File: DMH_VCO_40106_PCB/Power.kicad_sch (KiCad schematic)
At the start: 15 parts, among them J10 Panel_GND, J100 IDC_02x08, U1 40106, U2 TL074, U3 TL072

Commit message: Updates from testing on breadboard
- Removed Bus CV input, normalled it to V/oct input jack instead
- Renamed Lin FM input to Exp FM In 2
- Added annotations about temporary resistor/pot values
- Added annotations about pots and trimpots pinout
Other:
- company: (none) -> DMH Instruments
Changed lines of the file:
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@@
 	(generator_version "8.0")
 	(paper "A4")
+	(title_block
+		(company "DMH Instruments")
+	)
 	(junction
 		(at 142.24 31.75)

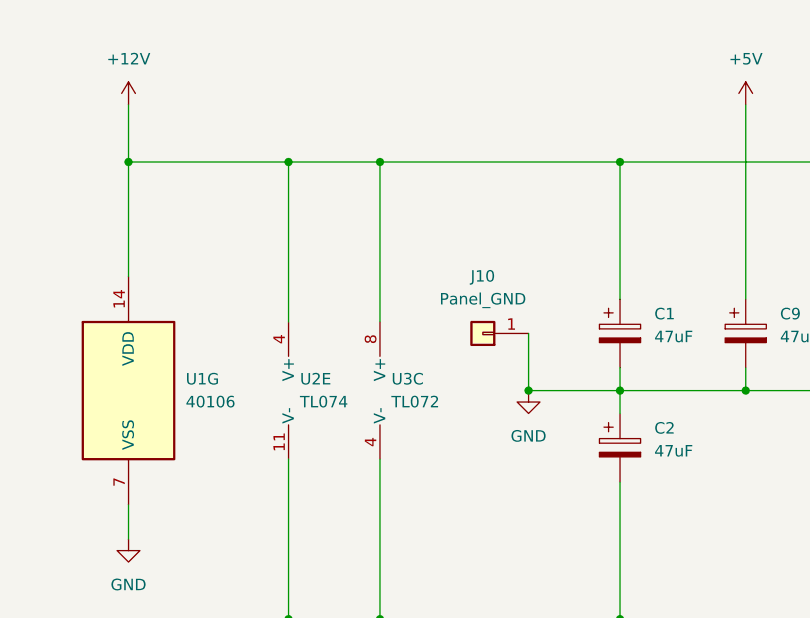
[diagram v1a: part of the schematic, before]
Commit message: Made U3 into TL074 instead of TL072
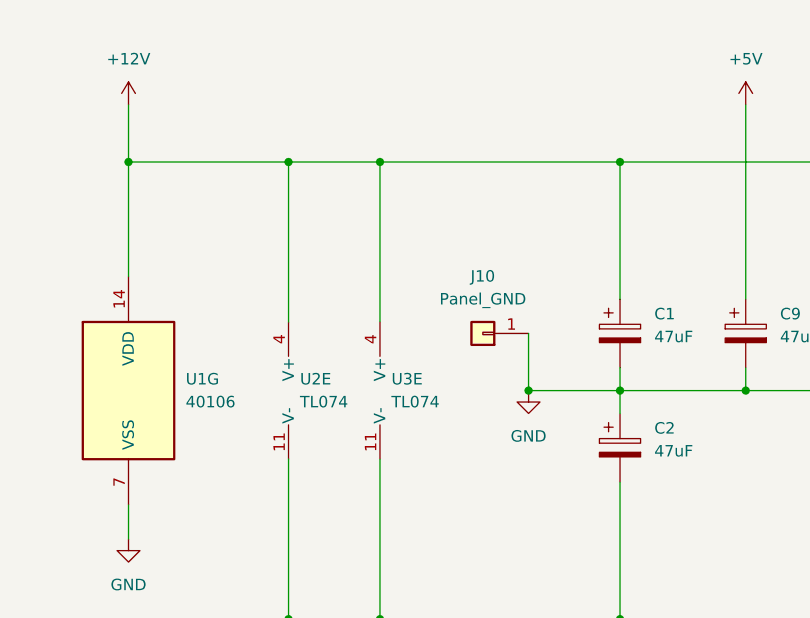
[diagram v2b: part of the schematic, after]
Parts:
- removed U3: TL072, Package_DIP:DIP-8_W7.62mm_Socket, symbol Amplifier_Operational:TL072
- added U3: TL074, symbol Amplifier_Operational:TL074
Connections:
- net +12V: now also U3.4 (V+)
- net -12V: now also U3.11 (V-)

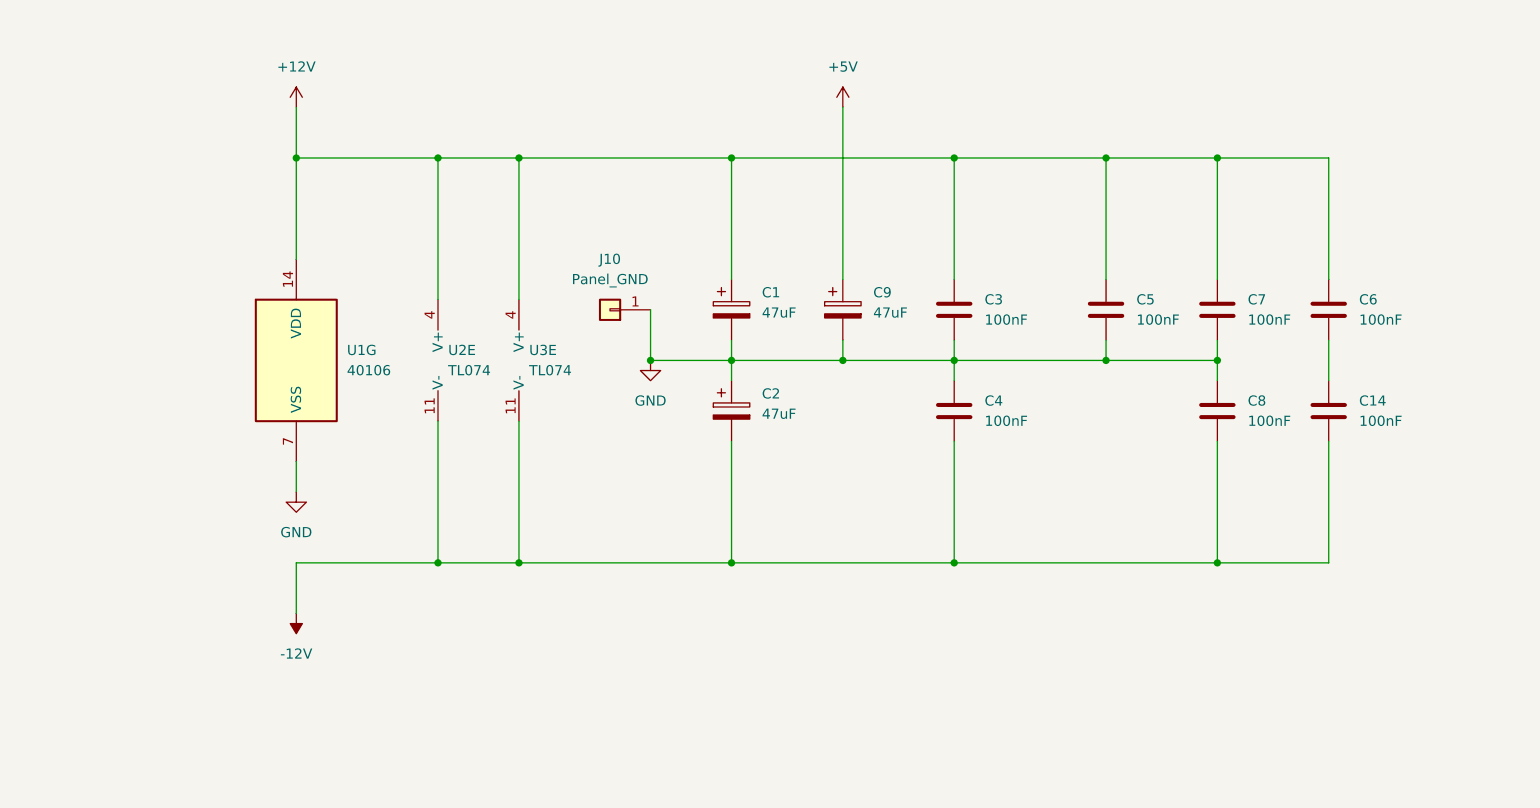
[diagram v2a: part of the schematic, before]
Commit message: Placed power for U4
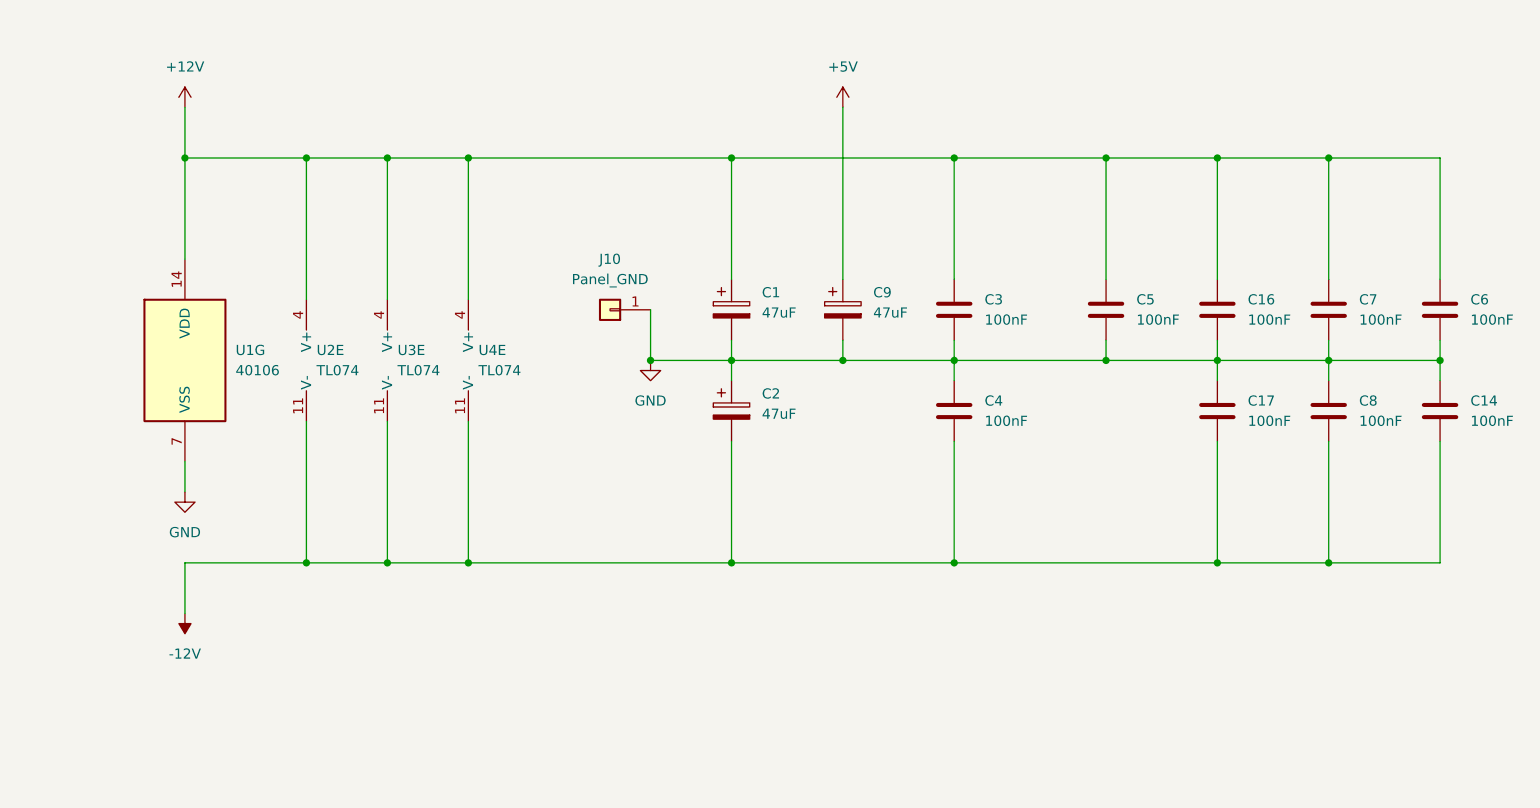
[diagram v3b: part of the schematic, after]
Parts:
- added C16, C17: 100nF, Capacitor_THT:C_Disc_D4.3mm_W1.9mm_P5.00mm, symbol Device:C
- added U4: TL074, symbol Amplifier_Operational:TL074
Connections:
- net +12V: now also C16.1, U4.4 (V+)
- net -12V: now also C17.2, U4.11 (V-)
- net GND: now also C14.1, C6.2, C16.2, C17.1
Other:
- moved on the sheet: C14, C6, C7, C8, U1G, U2E, U3E

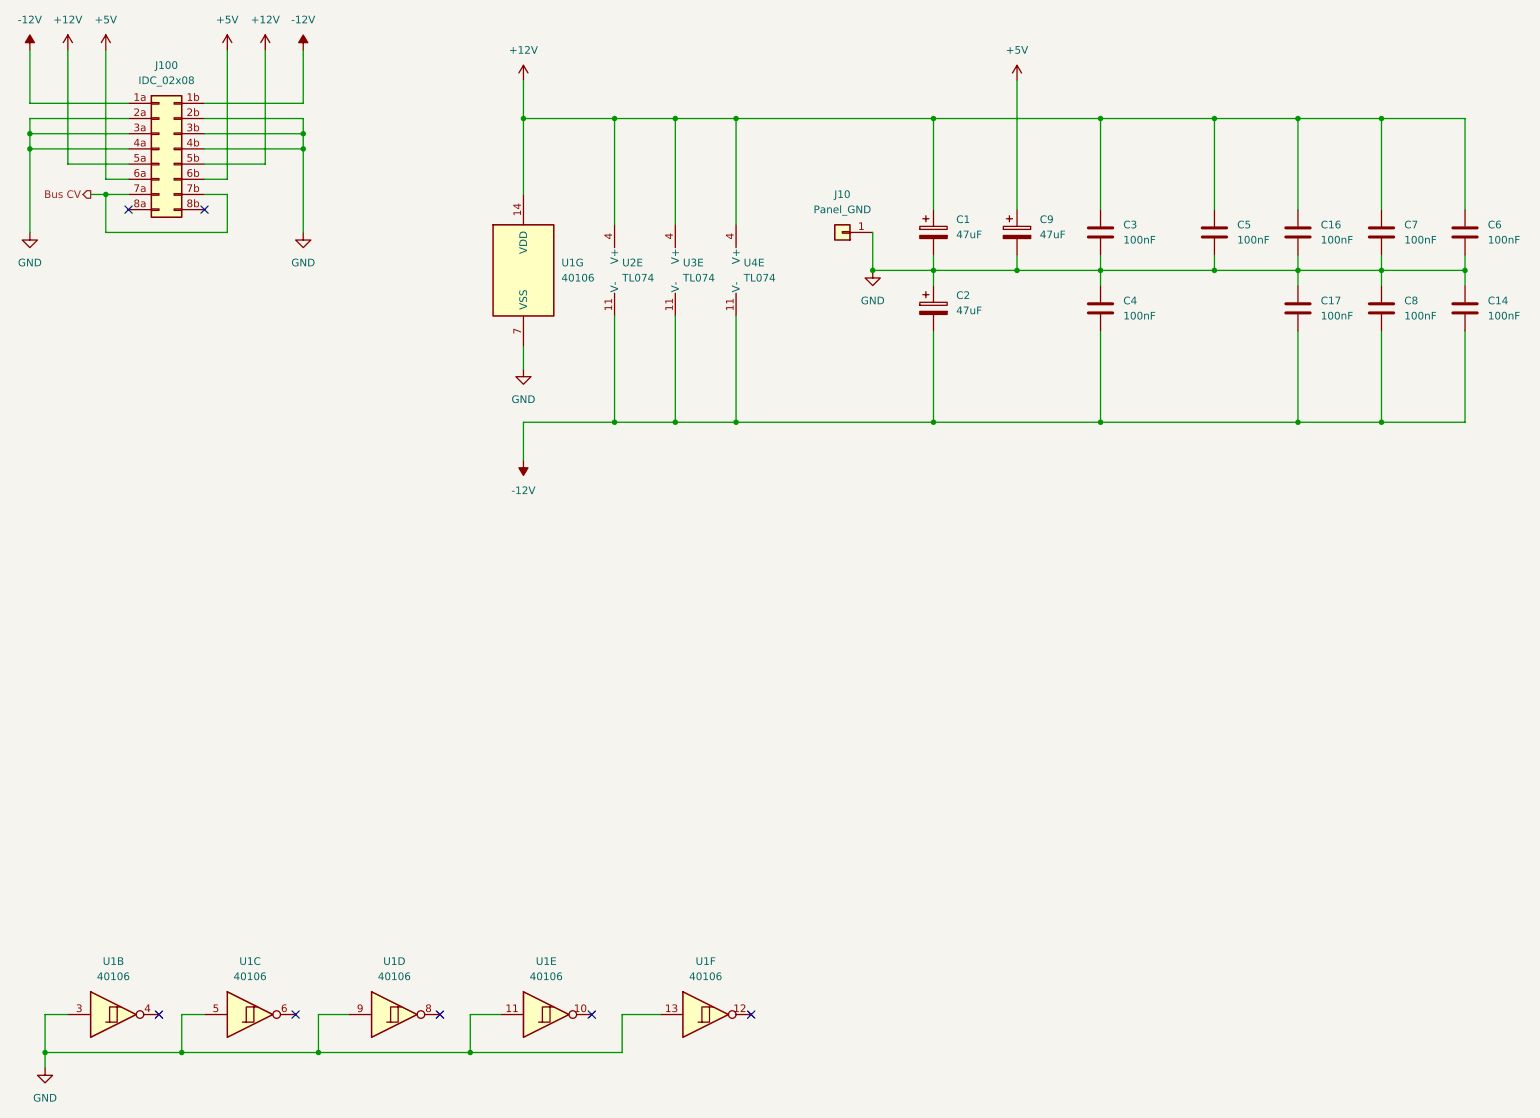
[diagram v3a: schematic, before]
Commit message: Organized power part and added protection diodes
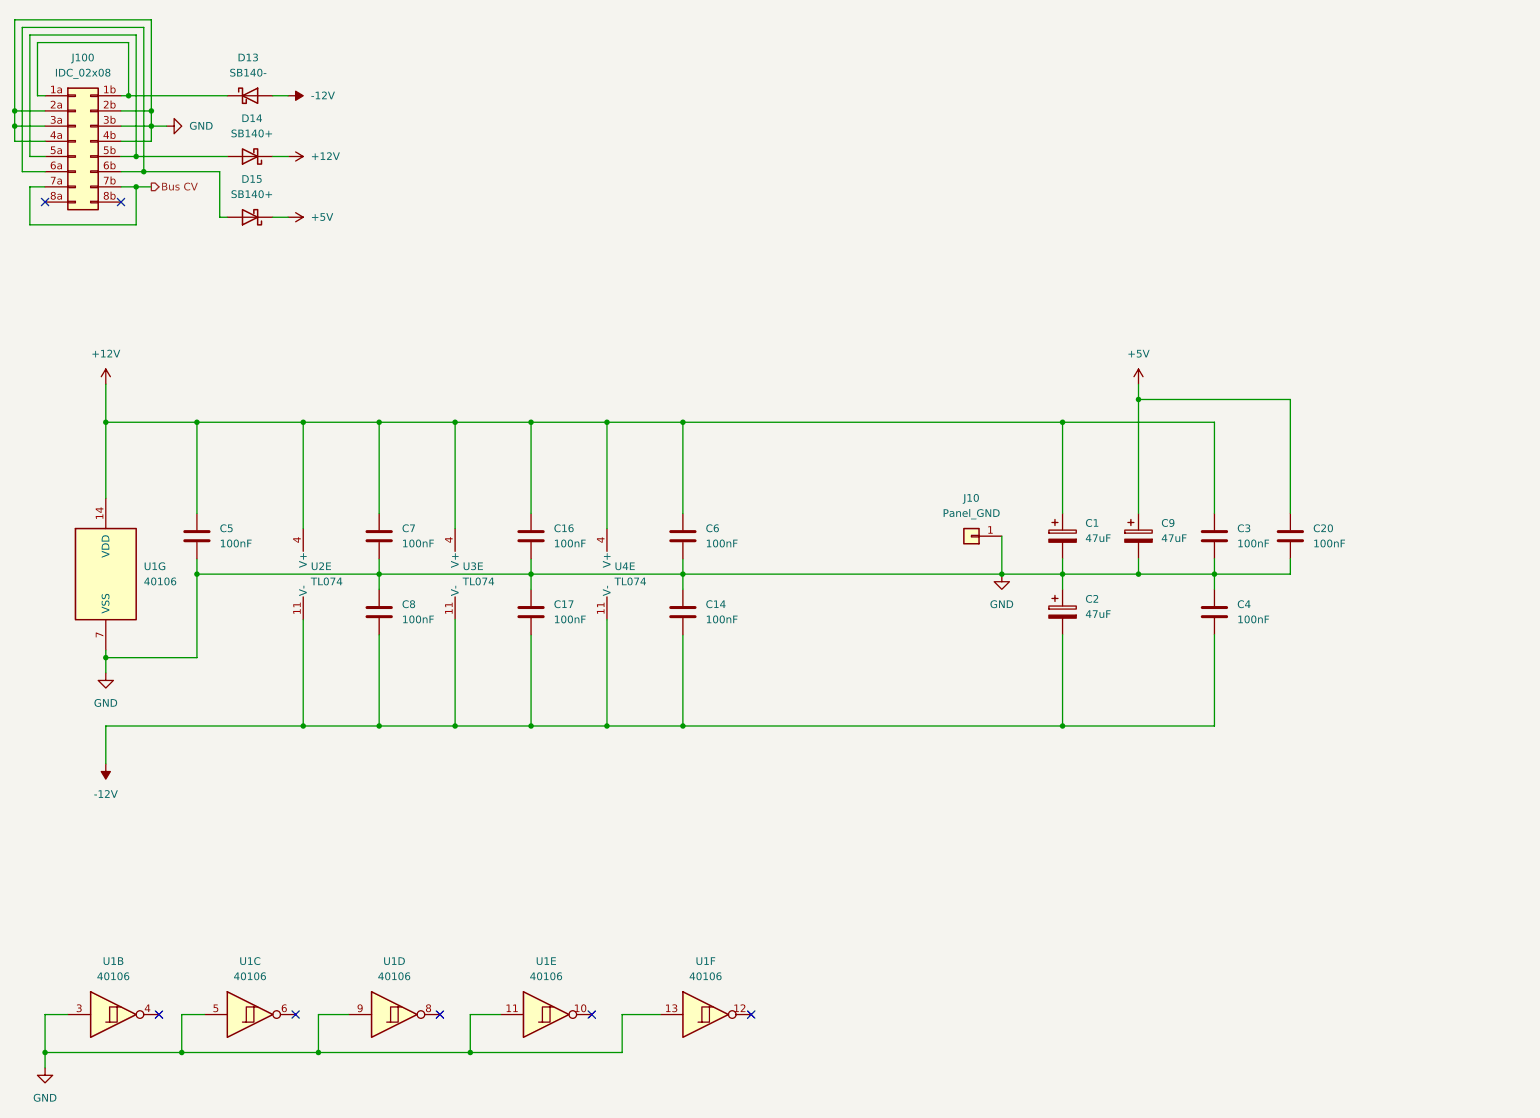
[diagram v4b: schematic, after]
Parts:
- added C20: 100nF, Capacitor_THT:C_Disc_D4.3mm_W1.9mm_P5.00mm, symbol Device:C
- added D13: SB140-, Diode_THT:D_DO-41_SOD81_P10.16mm_Horizontal, symbol SynthStuff:Power_Bus_Schotty_-
- added D14, D15: SB140+, Diode_THT:D_DO-41_SOD81_P10.16mm_Horizontal, symbol SynthStuff:Power_Bus_Schotty_+
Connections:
- net +12V: now also D14.1 (K); no longer J100.5a (Pin_5a), J100.5b (Pin_5b)
- net +5V: now also C20.1, D15.1 (K); no longer J100.6a (Pin_6a), J100.6b (Pin_6b)
- net -12V: now also D13.2 (A); no longer J100.1a (Pin_1a), J100.1b (Pin_1b)
- net GND: now also C20.2
- new net: D13.1 (K), J100.1a (Pin_1a), J100.1b (Pin_1b)
- new net: D14.2 (A), J100.5a (Pin_5a), J100.5b (Pin_5b)
- new net: D15.2 (A), J100.6a (Pin_6a), J100.6b (Pin_6b)
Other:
- moved on the sheet: C1, C14, C16, C17, C2, C3, C4, C5, C6, C7, C8, C9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

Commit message: Fixed trimpot fp linking
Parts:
- U3: footprint (none) -> Package_DIP:DIP-14_W7.62mm_Socket
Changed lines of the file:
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@@
 			)
 		)
-		(property "Footprint" ""
+		(property "Footprint" "Package_DIP:DIP-14_W7.62mm_Socket"
 			(at 90.17 105.41 0)
 			(effects

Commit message: Started positioning components on PCB
Moving some input resistores from main PCB to Jacks PCB
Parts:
- C9: footprint Capacitor_THT:CP_Radial_D4.0mm_P1.50mm -> Capacitor_THT:CP_Radial_D5.0mm_P2.00mm
- U4: footprint (none) -> Package_DIP:DIP-14_W7.62mm_Socket
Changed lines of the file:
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@@
 			)
 		)
-		(property "Footprint" ""
+		(property "Footprint" "Package_DIP:DIP-14_W7.62mm_Socket"
 			(at 115.57 105.41 0)
 			(effects
@@
 		)
 		(property "Description" "Quad Low-Noise JFET-Input Operational Amplifiers, DIP-14/SOIC-14"
+			(at 116.84 107.95 0)
+			(effects
+				(font
+					(size 1.27 1.27)
+				)
+				(hide yes)
+			)
+		)
+		(property "Function" ""
 			(at 116.84 107.95 0)
 			(effects
@@
 			)
 		)
-		(property "Footprint" "Capacitor_THT:CP_Radial_D4.0mm_P1.50mm"
+		(property "Footprint" "Capacitor_THT:CP_Radial_D5.0mm_P2.00mm"
 			(at 204.1652 105.41 0)
 			(effects
@@
 			(at 175.26 101.6 0)
 			(effects
+				(font
+					(size 1.27 1.27)
+				)
+				(hide yes)
+			)
+		)
+		(property "Function" ""
+			(at 175.26 101.6 0)
+			(effects
